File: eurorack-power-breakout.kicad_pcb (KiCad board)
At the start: 2 copper layers, 22.9 x 54.6 mm, 24 parts, among them J1 upper, J2 lower, J3 bus, J4 PWR, SW1 SW_SPDT

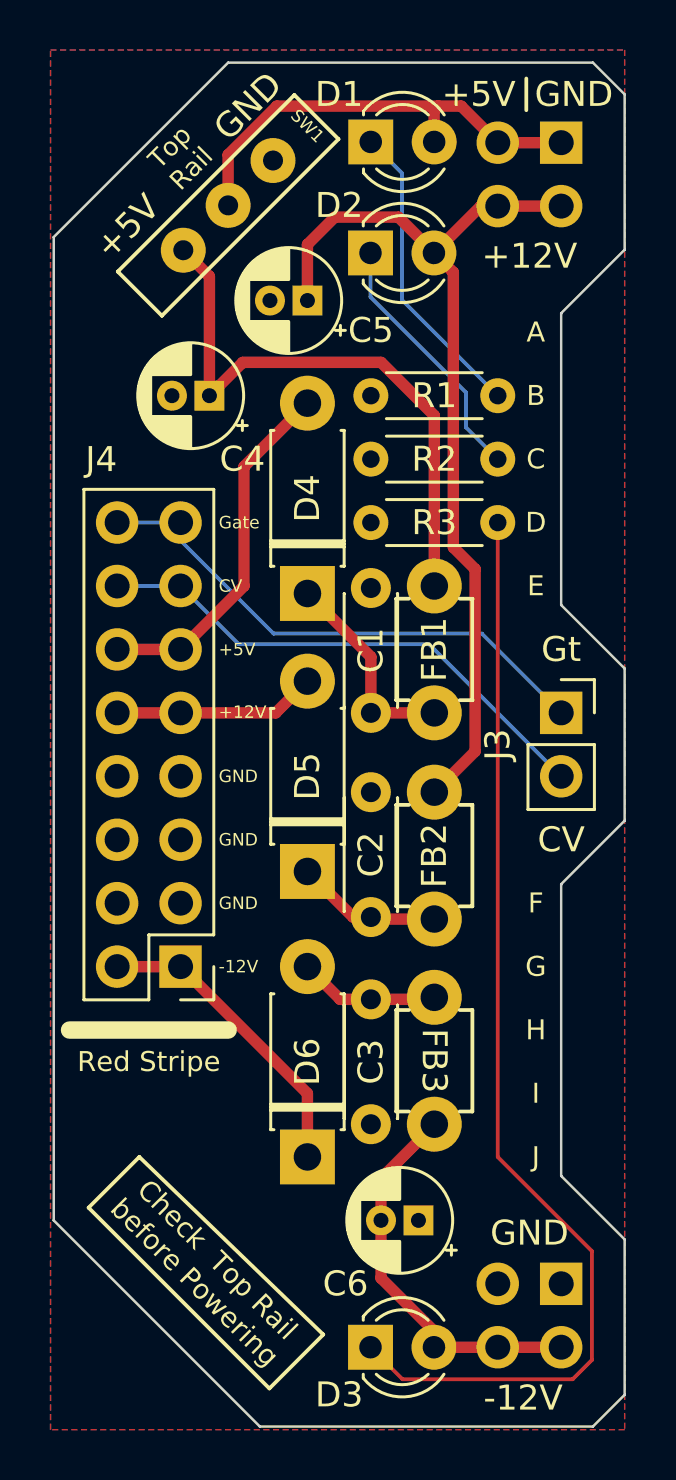
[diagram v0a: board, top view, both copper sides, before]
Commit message: :bug: Fix spacing on PCB-breadboard edge
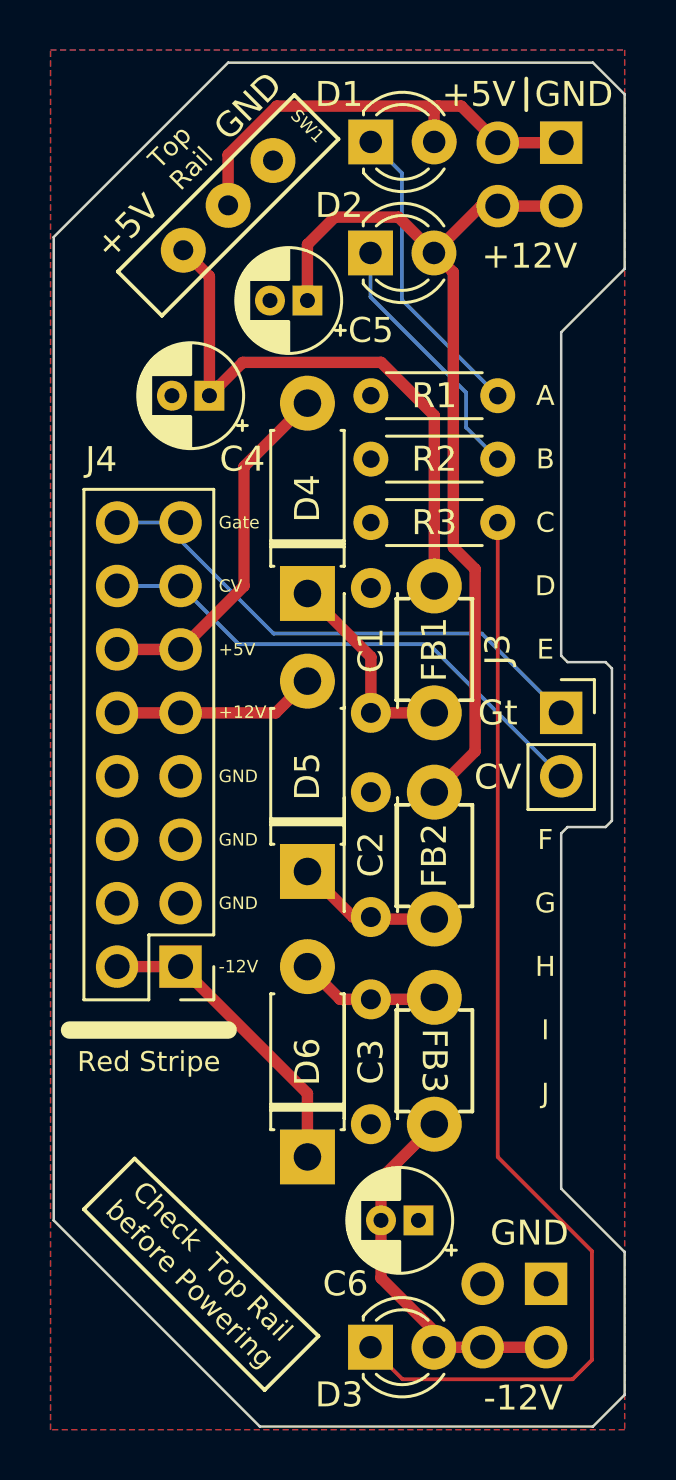
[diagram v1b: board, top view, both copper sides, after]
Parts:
- moved J2 0.60 mm to (146.7, 132.1)
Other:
- outline, holes or cut-outs redrawn

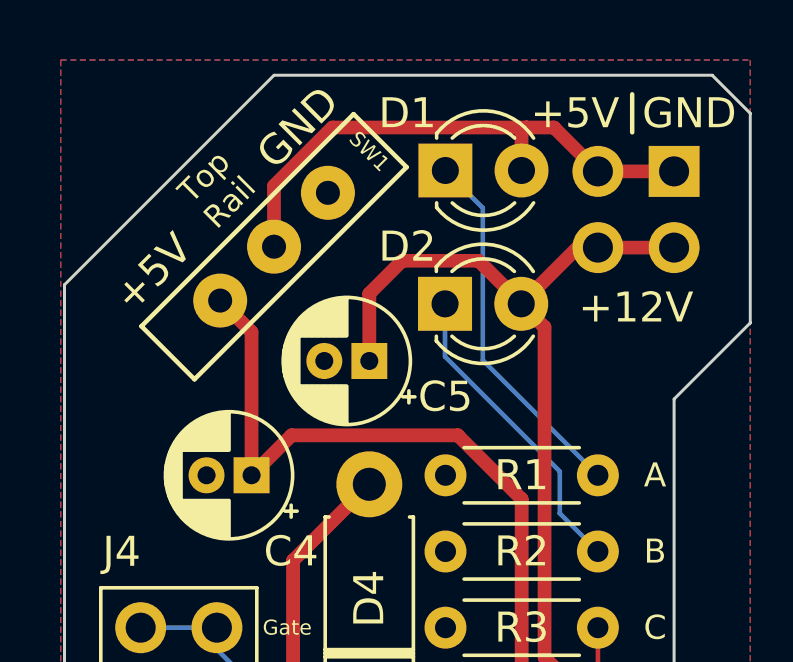
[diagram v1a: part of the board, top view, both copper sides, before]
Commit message: :art: Center the slide switch on the border
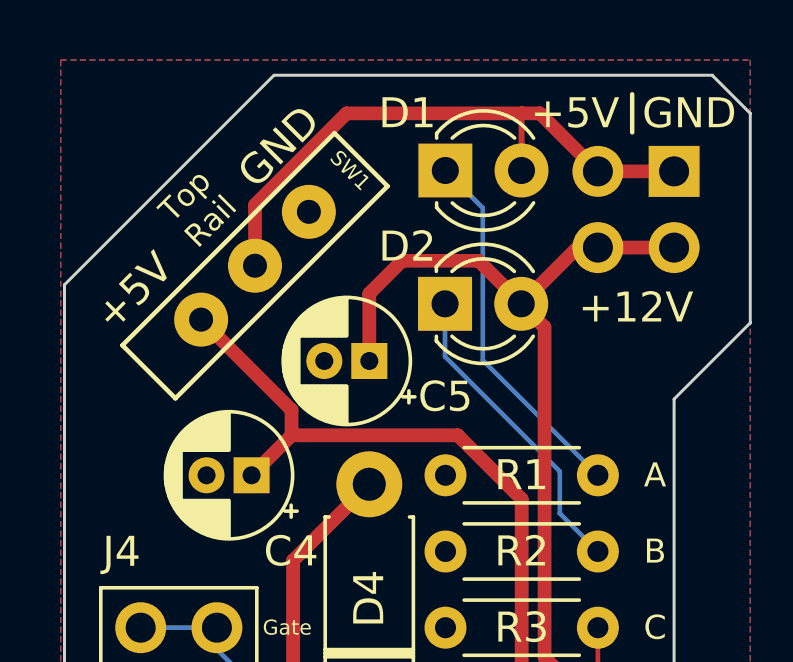
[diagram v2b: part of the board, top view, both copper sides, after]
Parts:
- moved SW1 0.90 mm to (133.3, 89.5)
- moved REF** 0.90 mm to (131.3, 91.6)
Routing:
- net 5Vselect: track 18.3 -> 20.0 mm
- net +5V: track 23.5 -> 22.4 mm
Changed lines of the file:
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@@
   )
   (footprint "mopsy:Switch_SPDT_NK236" (layer "F.Cu")
-    (at 133.985 88.9 45)
+    (at 133.35 89.535 45)
     (property "REICHELT" "NK 236")
     (property "Sheetfile" "eurorack-power-breakout.kicad_sch")
@@
   )
   (footprint "Symbol:OSHW-Symbol_6.7x6mm_SilkScreen" (layer "B.Cu")
-    (at 131.953 90.932 -45)
+    (at 131.318 91.567 -45)
     (descr "Open Source Hardware Symbol")
     (tags "Logo Symbol OSHW")
@@
     (effects (font (size 1 1) (thickness 0.15)))
   )
-  (gr_text "Top\nRail" (at 132.08 86.995 45) (layer "F.SilkS")
+  (gr_text "Top\nRail" (at 131.445 87.63 45) (layer "F.SilkS")
     (effects (font (size 0.75 0.75) (thickness 0.125)))
   )
-  (gr_text "GND" (at 135.89 83.82 45) (layer "F.SilkS")
+  (gr_text "GND" (at 135.255 84.455 45) (layer "F.SilkS")
     (effects (font (size 1 1) (thickness 0.15)) (justify right))
   )
@@
     (effects (font (size 0.5 0.5) (thickness 0.125)) (justify left))
   )
-  (gr_text "+5V" (at 128.905 90.805 45) (layer "F.SilkS")
+  (gr_text "+5V" (at 128.27 91.44 45) (layer "F.SilkS")
     (effects (font (size 1 1) (thickness 0.15)) (justify left))
   )
@@
   (segment (start 138.47 120.69) (end 137.16 119.38) (width 0.4572) (layer "F.Cu") (net 4))
   (segment (start 142.16 120.69) (end 142.24 120.61) (width 0.4572) (layer "F.Cu") (net 4))
+  (segment (start 131.553949 91.331051) (end 134.5684 94.345502) (width 0.4572) (layer "F.Cu") (net 5))
+  (segment (start 134.5684 94.345502) (end 134.5684 95.1866) (width 0.4572) (layer "F.Cu") (net 5))
   (segment (start 142.24 97.315708) (end 140.110892 95.1866) (width 0.4572) (layer "F.Cu") (net 5))
   (segment (start 140.110892 95.1866) (end 134.5684 95.1866) (width 0.4572) (layer "F.Cu") (net 5))
   (segment (start 134.5684 95.1866) (end 133.235 96.52) (width 0.4572) (layer "F.Cu") (net 5))
   (segment (start 142.24 104.14) (end 142.24 97.315708) (width 0.4572) (layer "F.Cu") (net 5))
-  (segment (start 132.188949 90.696051) (end 133.235 91.742102) (width 0.4572) (layer "F.Cu") (net 5))
-  (segment (start 133.235 91.742102) (end 133.235 96.52) (width 0.4572) (layer "F.Cu") (net 5))
   (segment (start 137.16 90.4632) (end 138.2516 89.3716) (width 0.4572) (layer "F.Cu") (net 6))
   (segment (start 138.2516 89.3716) (end 140.8066 89.3716) (width 0.4572) (layer "F.Cu") (net 6))
@@
   (segment (start 137.16 124.46) (end 137.16 127) (width 0.4572) (layer "F.Cu") (net 13))
   (segment (start 132.08 119.38) (end 137.16 124.46) (width 0.4572) (layer "F.Cu") (net 13))
-  (segment (start 142.235 85.095) (end 142.4034 84.9266) (width 0.4572) (layer "F.Cu") (net 14))
-  (segment (start 143.3166 84.9266) (end 144.78 86.39) (width 0.4572) (layer "F.Cu") (net 14))
-  (segment (start 133.985 86.872866) (end 135.931266 84.9266) (width 0.4572) (layer "F.Cu") (net 14))
+  (segment (start 136.402866 84.455) (end 142.24 84.455) (width 0.4572) (layer "F.Cu") (net 14))
+  (segment (start 133.35 89.535) (end 133.35 87.507866) (width 0.4572) (layer "F.Cu") (net 14))
+  (segment (start 142.235 84.46) (end 142.24 84.455) (width 0.4572) (layer "F.Cu") (net 14))
+  (segment (start 142.845 84.455) (end 144.78 86.39) (width 0.4572) (layer "F.Cu") (net 14))
   (segment (start 144.78 86.39) (end 147.32 86.39) (width 0.4572) (layer "F.Cu") (net 14))
-  (segment (start 133.985 88.9) (end 133.985 86.872866) (width 0.4572) (layer "F.Cu") (net 14))
-  (segment (start 135.931266 84.9266) (end 142.4034 84.9266) (width 0.4572) (layer "F.Cu") (net 14))
-  (segment (start 142.4034 84.9266) (end 143.3166 84.9266) (width 0.4572) (layer "F.Cu") (net 14))
-  (segment (start 142.235 86.36) (end 142.235 85.095) (width 0.4572) (layer "F.Cu") (net 14))
+  (segment (start 142.235 86.36) (end 142.235 84.46) (width 0.2032) (layer "F.Cu") (net 14))
+  (segment (start 142.24 84.455) (end 142.845 84.455) (width 0.4572) (layer "F.Cu") (net 14))
+  (segment (start 133.35 87.507866) (end 136.402866 84.455) (width 0.4572) (layer "F.Cu") (net 14))
   (segment (start 144.145 106.045) (end 147.32 109.22) (width 0.1524) (layer "B.Cu") (net 15))
   (segment (start 132.08 101.6) (end 132.08 102.322) (width 0.1524) (layer "B.Cu") (net 15))
@@
     )
   )
+  (group "" (id 328a3e07-e919-466a-ba37-5dcbd587bbaa)
+    (members
+      2433a415-cccf-47cb-b92e-a6df7b3b5b29
+      34a7ac5c-71e3-4539-9024-c5e5a928339d
+      616f80a0-df34-4eeb-ac04-ad06a7ae1ddd
+      a37a2192-4fdb-4eed-aa01-6a753eeadaff
+    )
+  )

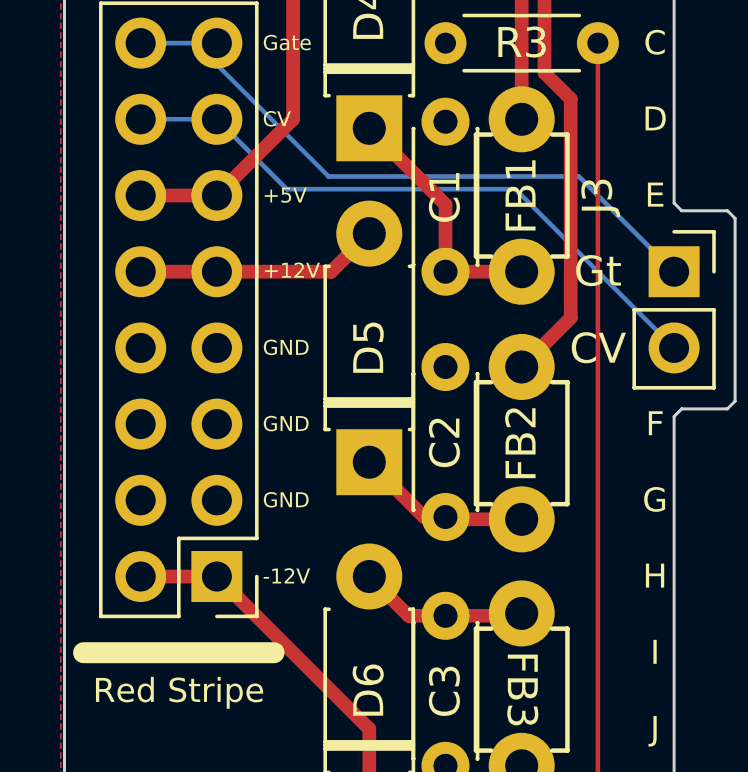
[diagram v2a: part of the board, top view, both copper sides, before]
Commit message: :art: Make labels on Bus socket shorter
It is still unclear if these labels will be visible. We will find out
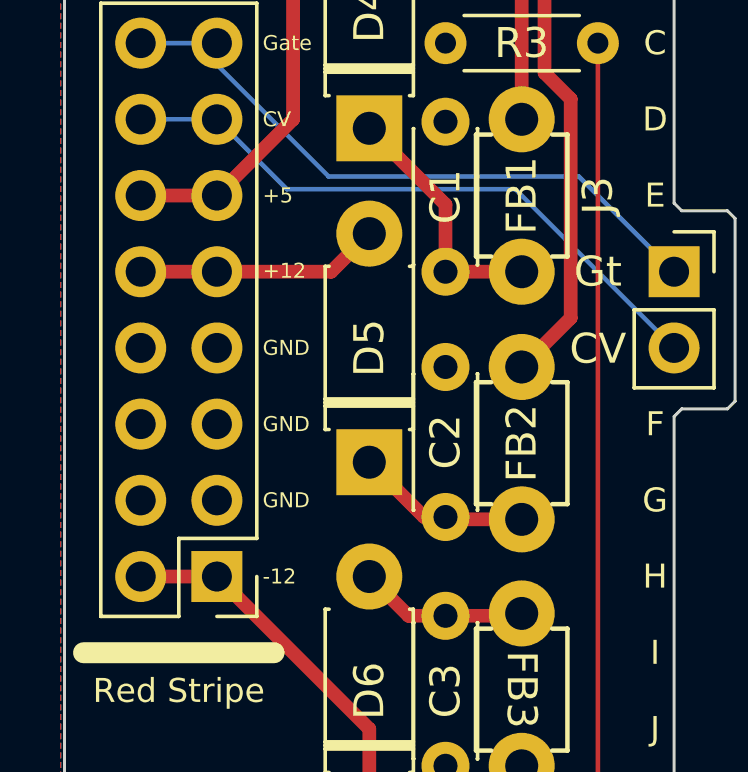
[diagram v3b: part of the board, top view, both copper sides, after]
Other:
- board text added: "+12"
- board text added: "+5"
- board text added: "-12"
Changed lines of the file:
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@@
     (effects (font (size 1 1) (thickness 0.15)))
   )
-  (gr_text "+12V" (at 133.604 109.19) (layer "F.SilkS")
+  (gr_text "+12" (at 133.604 109.19) (layer "F.SilkS")
     (effects (font (size 0.5 0.5) (thickness 0.125)) (justify left))
   )
@@
     (effects (font (size 0.5 0.5) (thickness 0.125)) (justify left))
   )
-  (gr_text "-12V" (at 133.604 119.38) (layer "F.SilkS")
+  (gr_text "-12" (at 133.604 119.38) (layer "F.SilkS")
     (effects (font (size 0.5 0.5) (thickness 0.125)) (justify left))
   )
@@
     (effects (font (size 0.5 0.5) (thickness 0.125)) (justify left))
   )
-  (gr_text "+5V" (at 133.604 106.68) (layer "F.SilkS")
+  (gr_text "+5" (at 133.604 106.68) (layer "F.SilkS")
     (effects (font (size 0.5 0.5) (thickness 0.125)) (justify left))
   )

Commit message: :sparkles: Add rivision marker and board meta data
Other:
- board text added: "v1"
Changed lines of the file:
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@@
   )
   (paper "A4")
+  (title_block
+    (title "Eurorack Power Breakout")
+    (date "2023-01-06")
+    (rev "v1")
+    (company "moPsy")
+  )
   (layers
     (0 "F.Cu" signal)
@@
   (gr_line (start 127 90.17) (end 127 129.54) (layer "Edge.Cuts") (width 0.1))
   (gr_line (start 149.352 113.538) (end 149.098 113.792) (layer "Edge.Cuts") (width 0.1))
+  (gr_text "v1" (at 136.525 135.255 90) (layer "B.SilkS")
+    (effects (font (size 0.8 0.8) (thickness 0.1)) (justify mirror))
+  )
   (gr_text "https://github.com/moPsy-project/eurorack-power-breakout" (at 134.62 116.84 90) (layer "B.SilkS")
     (effects (font (size 0.8 0.8) (thickness 0.1)) (justify mirror))
